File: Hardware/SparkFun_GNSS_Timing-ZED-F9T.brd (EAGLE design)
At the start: 43.2 x 43.2 mm, 144 parts, among them J1 Radio, J2 Qwiic Right Angle, J3 PTH, J4 Qwiic Right Angle, J5 USB Female Type C Connector, U3 U-BLOX_ZED_F9T, U5 AP2112K-3.3V

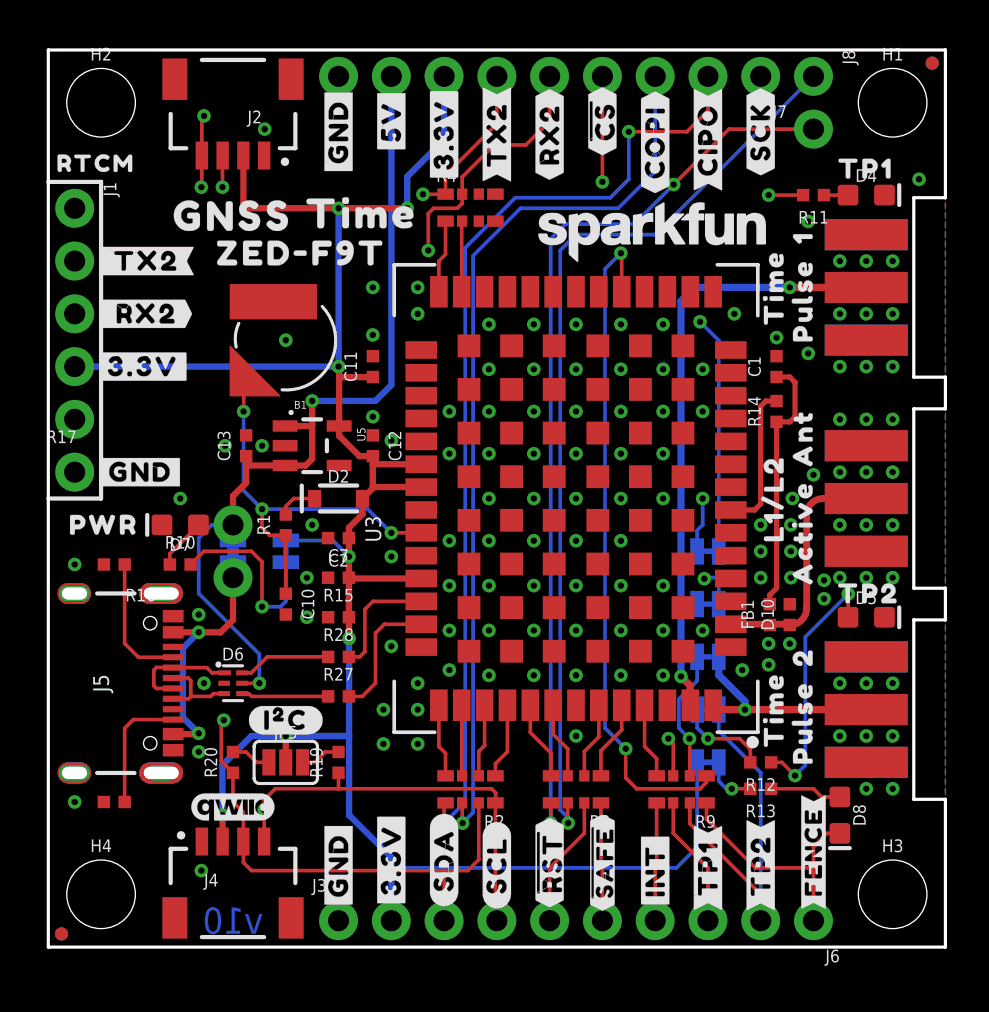
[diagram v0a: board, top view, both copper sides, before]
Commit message: Change RF trace width and other small changes from design review.
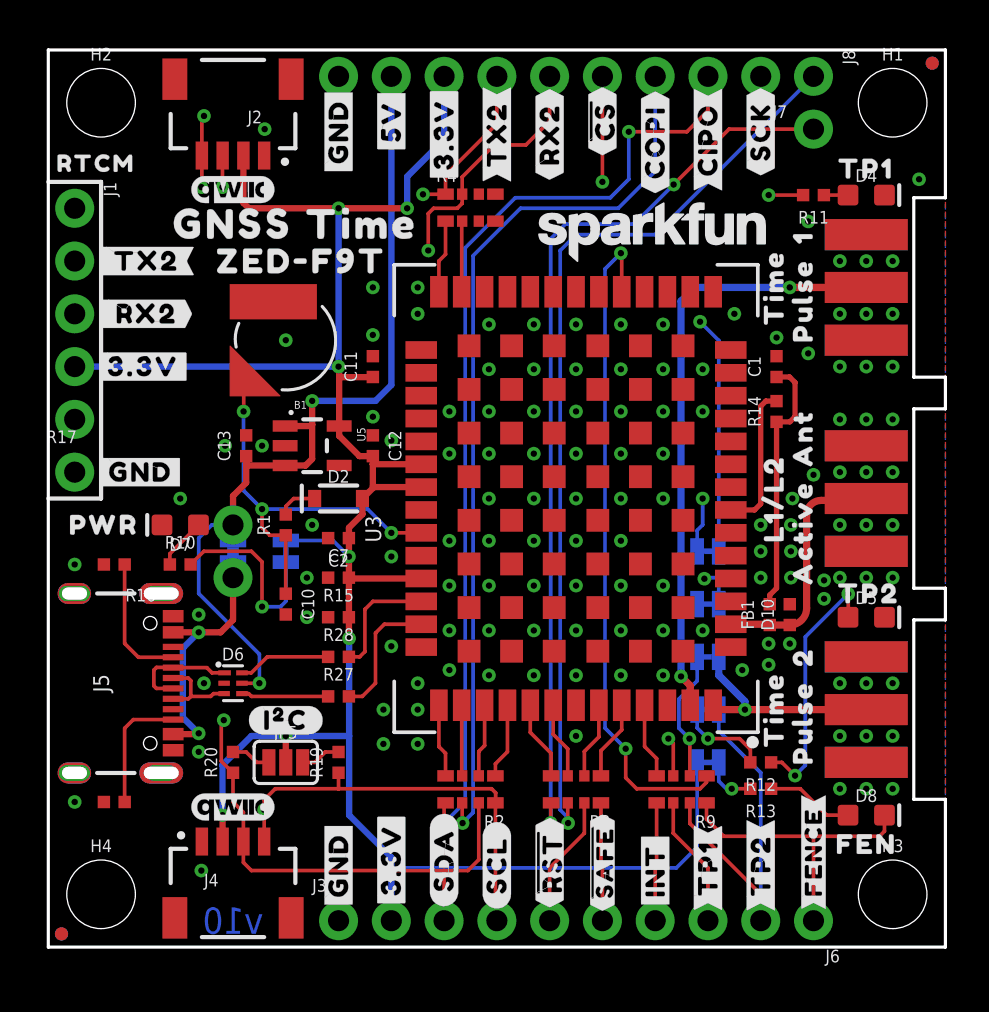
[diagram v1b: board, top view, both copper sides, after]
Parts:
- added LOGO3: QWIIC_LOGO_4MM, SparkFun-Aesthetics:QWIIC_4MM
- added U$78: (no value), output:FEN0
- moved D8 1.27 mm to (39.4, 6.35), turned to 0 degrees
- moved U$71 0.51 mm to (15.1, 34.8)
- moved U$34 0.38 mm to (12.2, 33.0)
- moved U$70 0.38 mm to (8.89, 34.8)
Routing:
- net FENCE_STAT: track 12.0 -> 14.6 mm
- net N$18: track 3.47 -> 4.23 mm
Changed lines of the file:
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@@
 <layers>
 <layer number="1" name="Top/Horz" color="4" fill="1" visible="yes" active="yes"/>
-<layer number="2" name="GND/Horz" color="1" fill="3" visible="no" active="yes"/>
-<layer number="15" name="Vert" color="4" fill="6" visible="no" active="yes"/>
+<layer number="2" name="GND/Horz" color="1" fill="3" visible="yes" active="yes"/>
+<layer number="15" name="Vert" color="4" fill="6" visible="yes" active="yes"/>
 <layer number="16" name="Bottom/Vert" color="1" fill="1" visible="yes" active="yes"/>
 <layer number="17" name="Pads" color="2" fill="1" visible="yes" active="yes"/>
@@
 <layer number="37" name="tTest" color="7" fill="1" visible="no" active="yes"/>
 <layer number="38" name="bTest" color="7" fill="1" visible="no" active="yes"/>
-<layer number="39" name="tKeepout" color="4" fill="11" visible="no" active="yes"/>
+<layer number="39" name="tKeepout" color="4" fill="11" visible="yes" active="yes"/>
 <layer number="40" name="bKeepout" color="1" fill="11" visible="no" active="yes"/>
 <layer number="41" name="tRestrict" color="4" fill="10" visible="no" active="yes"/>
@@
 <layer number="47" name="Measures" color="7" fill="1" visible="no" active="yes"/>
 <layer number="48" name="Document" color="7" fill="1" visible="no" active="yes"/>
-<layer number="49" name="Reference" color="7" fill="1" visible="no" active="yes"/>
+<layer number="49" name="Reference" color="7" fill="1" visible="yes" active="yes"/>
 <layer number="50" name="dxf" color="7" fill="1" visible="no" active="yes"/>
 <layer number="51" name="tDocu" color="6" fill="1" visible="yes" active="yes"/>
@@
 <class number="2" name="3.3V" width="0.508" drill="0.3048">
 </class>
-<class number="3" name="RF" width="0.33" drill="0">
+<class number="3" name="RF" width="0.349" drill="0">
 <clearance class="3" value="0.2032"/>
 </class>
@@
 <attribute name="VALUE" x="34.29" y="9.652" size="0.6096" layer="27" font="vector" ratio="20" rot="R180" align="top-center"/>
 </element>
-<element name="D8" library="SparkFun-LED" package="LED-0603" value="BLU" x="38.1" y="6.35" smashed="yes" rot="R270">
-<attribute name="NAME" x="38.735" y="6.35" size="0.6096" layer="25" font="vector" ratio="20" rot="R270" align="bottom-center"/>
-<attribute name="PROD_ID" value="DIO-08575" x="26.67" y="19.05" size="1.778" layer="27" font="vector" ratio="15" rot="R270" display="off"/>
-<attribute name="VALUE" x="37.465" y="6.35" size="0.6096" layer="27" font="vector" ratio="20" rot="R270" align="top-center"/>
+<element name="D8" library="SparkFun-LED" package="LED-0603" value="BLU" x="39.37" y="6.35" smashed="yes">
+<attribute name="NAME" x="39.37" y="6.985" size="0.6096" layer="25" font="vector" ratio="20" align="bottom-center"/>
+<attribute name="PROD_ID" value="DIO-08575" x="26.67" y="-5.08" size="1.778" layer="27" font="vector" ratio="15" display="off"/>
+<attribute name="VALUE" x="39.37" y="5.715" size="0.6096" layer="27" font="vector" ratio="20" align="top-center"/>
 </element>
 <element name="FENCE" library="SparkFun-Jumpers" package="SMT-JUMPER_2_NC_TRACE_SILK" package3d_urn="urn:adsk.eagle:package:39281/1" value="JUMPER-SMT_2_NC_TRACE_SILK" x="31.75" y="8.89" smashed="yes" rot="MR0">
@@
 <element name="U$69" library="output" package="#I�C#0" value="" x="11.43" y="10.922" smashed="yes"/>
 <element name="LOGO4" library="SparkFun-Aesthetics" package="QWIIC_4MM" value="QWIIC_LOGO_4MM" x="8.89" y="6.731" smashed="yes"/>
-<element name="U$70" library="output" package="GNSS0" value="" x="8.89" y="35.179" smashed="yes"/>
-<element name="U$71" library="output" package="TIME1" value="" x="15.113" y="35.306" smashed="yes"/>
-<element name="U$34" library="output" package="ZED#F9T0" value="" x="12.192" y="33.401" smashed="yes"/>
+<element name="U$70" library="output" package="GNSS0" value="" x="8.89" y="34.798" smashed="yes"/>
+<element name="U$71" library="output" package="TIME1" value="" x="15.113" y="34.798" smashed="yes"/>
+<element name="U$34" library="output" package="ZED#F9T0" value="" x="12.192" y="33.02" smashed="yes"/>
 <element name="LOGO5" library="SparkFun-Aesthetics" package="SFE_LOGO_NAME_.1" value="SFE_LOGO_NAME.1_INCH" x="29.083" y="34.417" smashed="yes"/>
 <element name="U$72" library="output" package="##SAFE##0" value="" x="26.67" y="4.064" smashed="yes" rot="R90"/>
@@
 <element name="U$74" library="output" package="TIME1" value="" x="18.288" y="24.13" smashed="yes" rot="MR0"/>
 <element name="U$77" library="output" package="ZED#F9T0" value="" x="21.59" y="21.59" smashed="yes" rot="MR0"/>
+<element name="U$78" library="output" package="FEN0" value="" x="39.37" y="4.953" smashed="yes"/>
+<element name="LOGO3" library="SparkFun-Aesthetics" package="QWIIC_4MM" value="QWIIC_LOGO_4MM" x="8.89" y="36.449" smashed="yes"/>
 </elements>
 <signals>
@@
 <contactref element="D6" pad="2"/>
 <contactref element="E1" pad="GND@1"/>
-<polygon width="0.1524" layer="1" isolate="0.1524" rank="4">
+<polygon width="0.2032" layer="1" isolate="0.2032" rank="4">
 <vertex x="0" y="43.18"/>
 <vertex x="0" y="0"/>
@@
 <vertex x="43.18" y="43.18"/>
 </polygon>
-<polygon width="0.1524" layer="16" isolate="0.1524" rank="4">
+<polygon width="0.2032" layer="16" isolate="0.2032" rank="4">
 <vertex x="43.18" y="43.18"/>
 <vertex x="43.18" y="0"/>
@@
 <vertex x="0" y="43.18"/>
 </polygon>
-<polygon width="0.1524" layer="15" isolate="0.1524" rank="4">
+<polygon width="0.2032" layer="15" isolate="0.2032" rank="4">
 <vertex x="43.18" y="43.18"/>
 <vertex x="43.18" y="0"/>
@@
 <vertex x="0" y="43.18"/>
 </polygon>
-<polygon width="0.1524" layer="2" isolate="0.1524" rank="4">
+<polygon width="0.2032" layer="2" isolate="0.2032" rank="4">
 <vertex x="43.18" y="43.18"/>
 <vertex x="43.18" y="0"/>
@@
 <via x="25.4" y="10.16" extent="1-16" drill="0.3048"/>
 <via x="37.338" y="16.764" extent="1-16" drill="0.3048"/>
+<via x="38.1" y="7.62" extent="1-16" drill="0.3048"/>
 </signal>
 <signal name="TX1_LV">
@@
 <contactref element="D10" pad="1"/>
 <contactref element="U3" pad="2"/>
-<wire x1="35.649" y1="15.54" x2="35.687" y2="15.502" width="0.35" layer="1"/>
-<wire x1="35.649" y1="15.54" x2="35.687" y2="15.502" width="0.33" layer="1" curve="-90"/>
-<wire x1="36.5" y1="20.8" x2="37.29" y2="21.59" width="0.33" layer="1" curve="-90"/>
-<wire x1="37.29" y1="21.59" x2="39.37" y2="21.59" width="0.33" layer="1"/>
-<wire x1="32.85" y1="15.54" x2="34.687" y2="15.54" width="0.33" layer="1"/>
-<wire x1="34.687" y1="15.54" x2="34.725" y2="15.502" width="0.33" layer="1" curve="-90"/>
-<wire x1="34.725" y1="15.502" x2="34.763" y2="15.54" width="0.33" layer="1" curve="-90"/>
-<wire x1="34.763" y1="15.54" x2="35.649" y2="15.54" width="0.33" layer="1"/>
-<wire x1="35.687" y1="15.502" x2="36.5" y2="16.315" width="0.33" layer="1" curve="90"/>
-<wire x1="36.5" y1="16.315" x2="36.5" y2="20.8" width="0.33" layer="1"/>
+<wire x1="32.85" y1="15.54" x2="34.687" y2="15.54" width="0.349" layer="1"/>
+<wire x1="34.687" y1="15.54" x2="34.725" y2="15.502" width="0.349" layer="1" curve="-90"/>
+<wire x1="34.725" y1="15.502" x2="35.687" y2="15.502" width="0.349" layer="1"/>
+<wire x1="35.687" y1="15.502" x2="36.5" y2="16.315" width="0.349" layer="1" curve="90"/>
+<wire x1="36.5" y1="20.8" x2="37.2" y2="21.5" width="0.349" layer="1" curve="-90"/>
+<wire x1="37.2" y1="21.5" x2="39.28" y2="21.5" width="0.349" layer="1"/>
+<wire x1="39.28" y1="21.5" x2="39.37" y2="21.59" width="0.349" layer="1" curve="90"/>
+<wire x1="36.5" y1="16.315" x2="36.5" y2="20.8" width="0.349" layer="1"/>
 </signal>
 <signal name="N$11">
@@
 <contactref element="D8" pad="C"/>
 <wire x1="31.68" y1="6.94" x2="31.68" y2="6.166" width="0.1778" layer="1"/>
-<wire x1="34.036" y1="3.81" x2="36.83" y2="3.81" width="0.1778" layer="1"/>
-<wire x1="36.83" y1="3.81" x2="36.83" y2="1.27" width="0.1778" layer="1"/>
-<wire x1="31.68" y1="6.166" x2="34.036" y2="3.81" width="0.1778" layer="1"/>
-<wire x1="38.1" y1="5.473" x2="37.477" y2="5.473" width="0.1778" layer="1"/>
-<wire x1="37.477" y1="5.473" x2="36.83" y2="4.826" width="0.1778" layer="1"/>
-<wire x1="36.83" y1="4.826" x2="36.83" y2="3.81" width="0.1778" layer="1"/>
+<wire x1="31.68" y1="6.166" x2="32.512" y2="5.334" width="0.1778" layer="1"/>
+<wire x1="40.247" y1="6.35" x2="40.247" y2="5.576" width="0.1778" layer="1"/>
+<wire x1="40.247" y1="5.576" x2="40.005" y2="5.334" width="0.1778" layer="1"/>
+<wire x1="40.005" y1="5.334" x2="36.83" y2="5.334" width="0.1778" layer="1"/>
+<wire x1="36.83" y1="5.334" x2="32.512" y2="5.334" width="0.1778" layer="1"/>
+<wire x1="36.83" y1="1.27" x2="36.83" y2="5.334" width="0.1778" layer="1"/>
 </signal>
 <signal name="N$2">
@@
 <contactref element="D8" pad="A"/>
 <contactref element="R13" pad="1"/>
-<wire x1="38.1" y1="7.227" x2="37.223" y2="7.227" width="0.1778" layer="1"/>
-<wire x1="37.223" y1="7.227" x2="36.83" y2="7.62" width="0.1778" layer="1"/>
-<wire x1="36.83" y1="7.62" x2="34.79" y2="7.62" width="0.1778" layer="1"/>
+<wire x1="34.79" y1="7.62" x2="36.195" y2="7.62" width="0.1778" layer="1"/>
+<wire x1="38.493" y1="6.35" x2="37.465" y2="6.35" width="0.1778" layer="1"/>
+<wire x1="37.465" y1="6.35" x2="36.195" y2="7.62" width="0.1778" layer="1"/>
 </signal>
 <signal name="N$19">

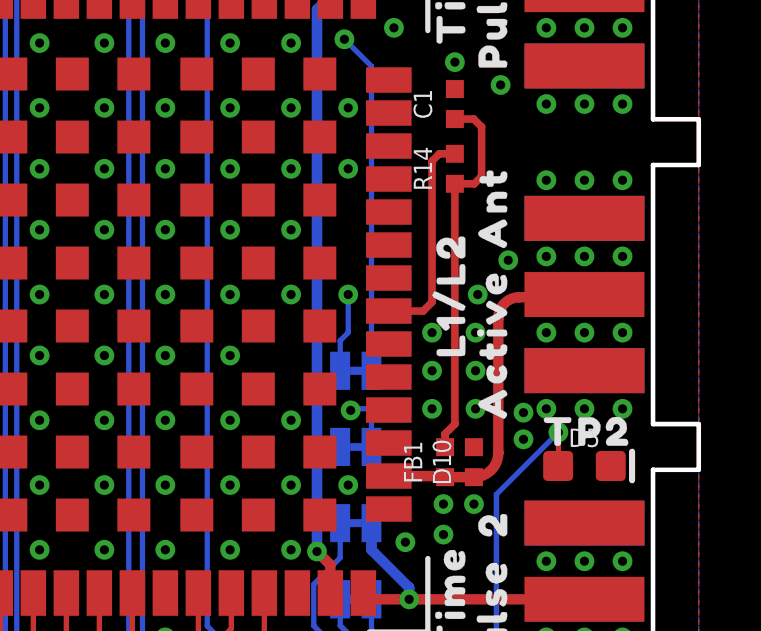
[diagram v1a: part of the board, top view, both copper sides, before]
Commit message: Add production panel.
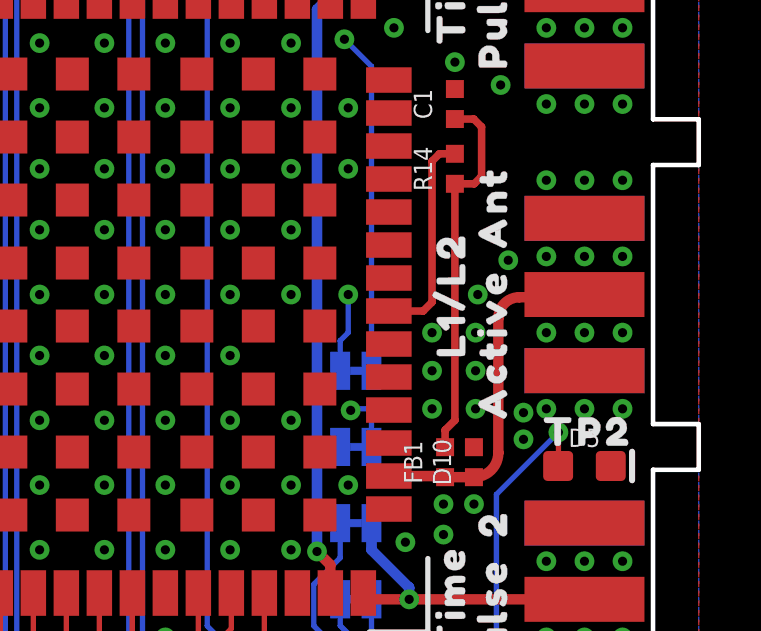
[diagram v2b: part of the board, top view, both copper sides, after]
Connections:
- net RXI/MOSI renamed RXI/COPI
- net TXO/MISO renamed TXO/CIPO
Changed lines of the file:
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@@
 <layers>
 <layer number="1" name="Top/Horz" color="4" fill="1" visible="yes" active="yes"/>
-<layer number="2" name="GND/Horz" color="1" fill="3" visible="yes" active="yes"/>
-<layer number="15" name="Vert" color="4" fill="6" visible="yes" active="yes"/>
+<layer number="2" name="GND/Horz" color="1" fill="3" visible="no" active="yes"/>
+<layer number="15" name="Vert" color="4" fill="6" visible="no" active="yes"/>
 <layer number="16" name="Bottom/Vert" color="1" fill="1" visible="yes" active="yes"/>
 <layer number="17" name="Pads" color="2" fill="1" visible="yes" active="yes"/>
@@
 <layer number="37" name="tTest" color="7" fill="1" visible="no" active="yes"/>
 <layer number="38" name="bTest" color="7" fill="1" visible="no" active="yes"/>
-<layer number="39" name="tKeepout" color="4" fill="11" visible="yes" active="yes"/>
+<layer number="39" name="tKeepout" color="4" fill="11" visible="no" active="yes"/>
 <layer number="40" name="bKeepout" color="1" fill="11" visible="no" active="yes"/>
 <layer number="41" name="tRestrict" color="4" fill="10" visible="no" active="yes"/>
@@
 <contactref element="C1" pad="1"/>
 <contactref element="FB1" pad="2"/>
-<wire x1="35.052" y1="25.281" x2="35.052" y2="17.272" width="0.254" layer="1"/>
+<wire x1="35.052" y1="25.281" x2="35.052" y2="17.399" width="0.254" layer="1"/>
 <wire x1="35.052" y1="27.44" x2="35.679" y2="27.44" width="0.254" layer="1"/>
 <wire x1="35.679" y1="27.44" x2="35.941" y2="27.178" width="0.254" layer="1"/>
@@
 <wire x1="35.941" y1="27.178" x2="35.941" y2="25.527" width="0.254" layer="1"/>
 <wire x1="35.941" y1="25.527" x2="35.695" y2="25.281" width="0.254" layer="1"/>
-<wire x1="34.725" y1="16.502" x2="34.725" y2="16.945" width="0.254" layer="1"/>
-<wire x1="34.725" y1="16.945" x2="35.052" y2="17.272" width="0.254" layer="1"/>
+<wire x1="34.725" y1="16.502" x2="34.725" y2="17.072" width="0.254" layer="1"/>
+<wire x1="34.725" y1="17.072" x2="35.052" y2="17.399" width="0.254" layer="1"/>
 </signal>
 <signal name="D+">
@@
 <wire x1="31.496" y1="20.32" x2="31.2293" y2="20.0533" width="0.1778" layer="16"/>
 </signal>
-<signal name="RXI/MOSI">
+<signal name="RXI/COPI">
 <contactref element="J7" pad="3"/>
 <contactref element="R2" pad="P6"/>
@@
 <wire x1="29.21" y1="37.338" x2="27.432" y2="35.56" width="0.1778" layer="16"/>
 </signal>
-<signal name="TXO/MISO">
+<signal name="TXO/CIPO">
 <contactref element="J7" pad="2"/>
 <contactref element="R2" pad="P5"/>
